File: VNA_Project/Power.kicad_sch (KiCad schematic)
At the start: 35 parts, among them J201 USB_C_Receptacle_USB2.0_16P, J202 Jack-DC, U201 AP7375, U202 USBLC6-2SC6, U203 TLV62569DBV, U204 HT7533-1, U6 MIC5501-3.0YM5

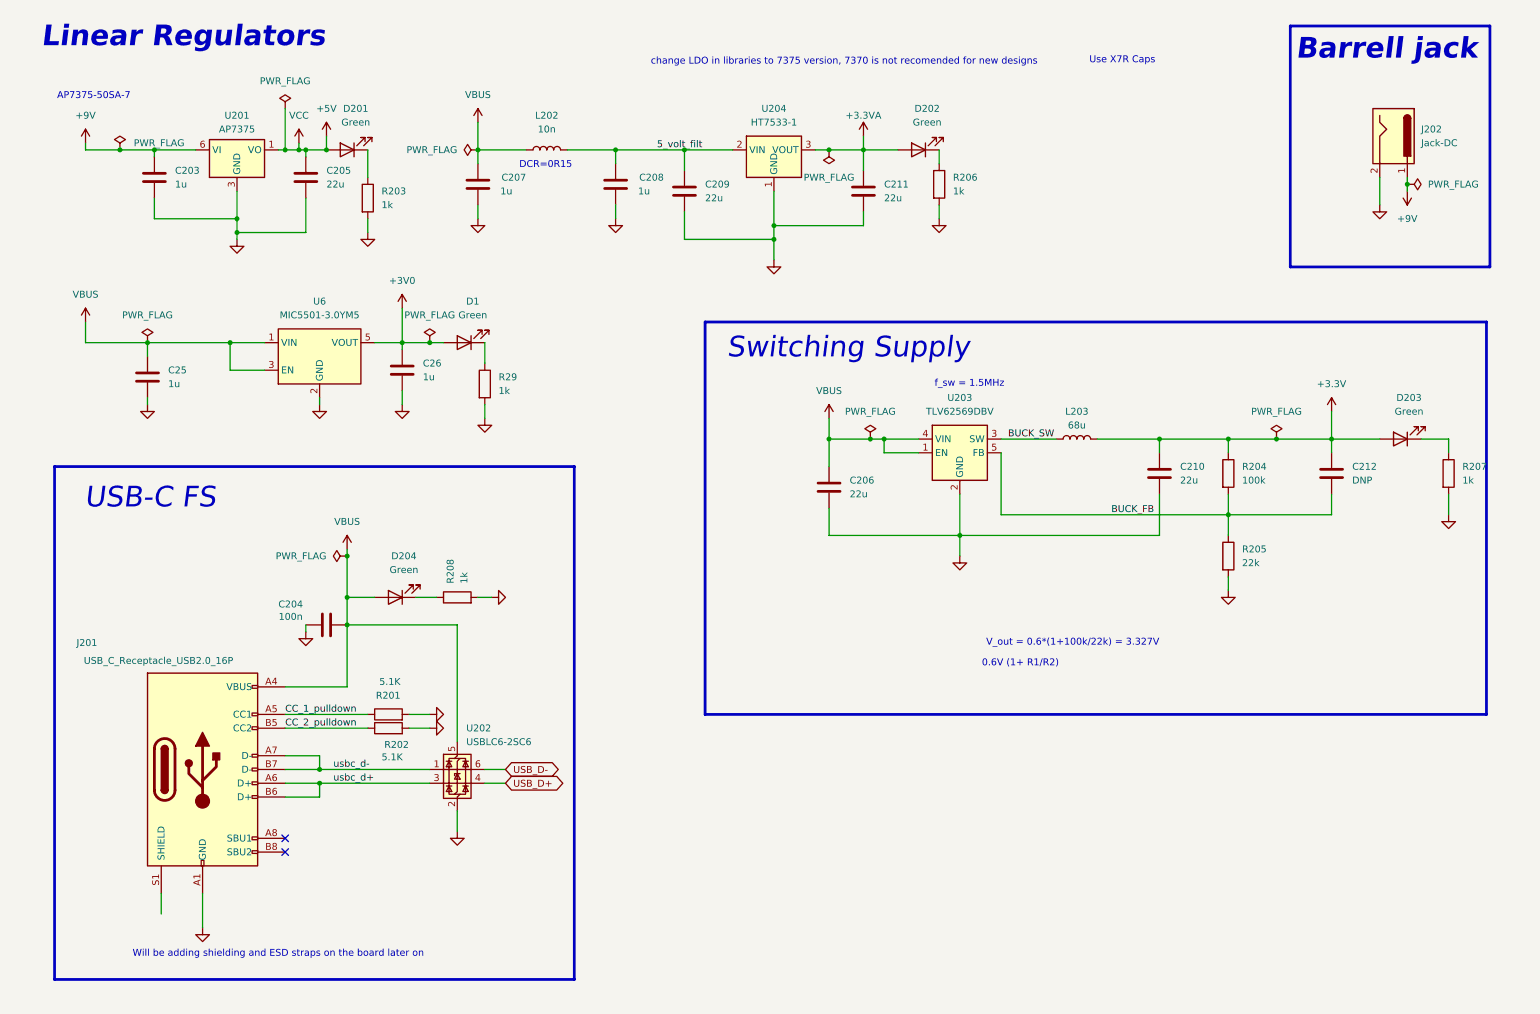
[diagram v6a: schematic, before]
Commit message: finishing up front end
refining Non RF front end
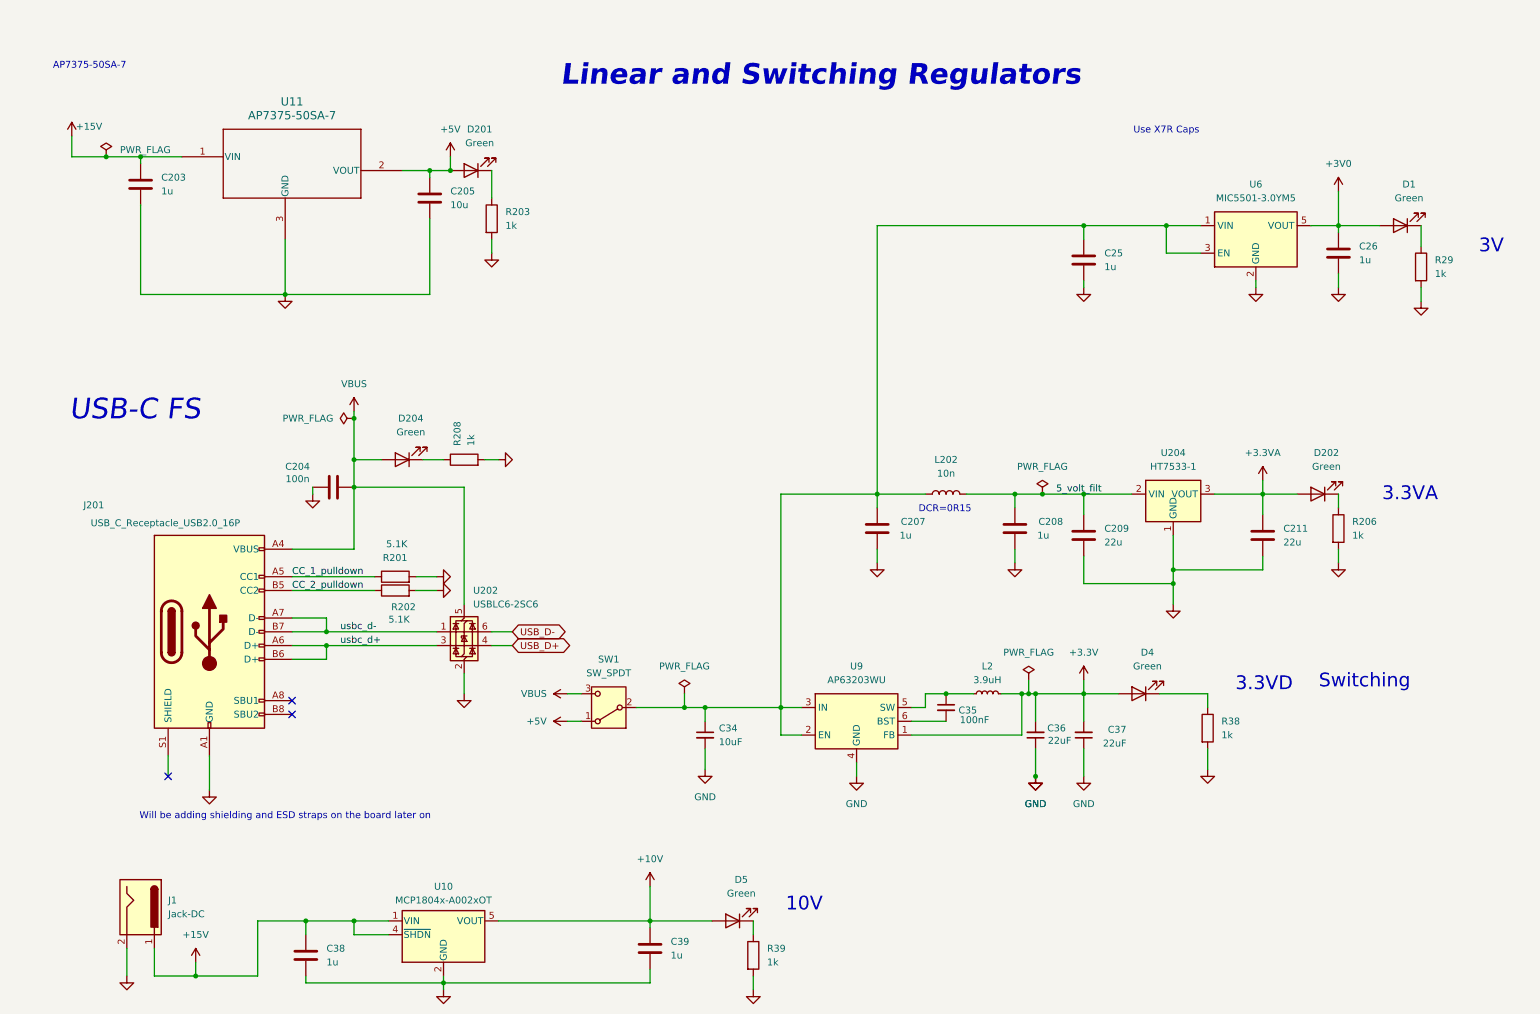
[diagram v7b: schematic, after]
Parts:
- removed C206, C210: 22u, Capacitor_SMD:C_0603_1608Metric_Pad1.08x0.95mm_HandSolder, symbol Device:C
- removed C212: DNP, Capacitor_SMD:C_0402_1005Metric_Pad0.74x0.62mm_HandSolder, symbol Device:C
- removed D203: Green, LED_SMD:LED_0402_1005Metric_Pad0.77x0.64mm_HandSolder, symbol Device:LED
- removed J202: Jack-DC, symbol Connector:Jack-DC
- removed L203: 68u, Inductor_SMD:L_0603_1608Metric_Pad1.05x0.95mm_HandSolder, symbol Device:L
- removed R204: 100k, Resistor_SMD:R_0402_1005Metric_Pad0.72x0.64mm_HandSolder, symbol Device:R
- removed R205: 22k, Resistor_SMD:R_0402_1005Metric_Pad0.72x0.64mm_HandSolder, symbol Device:R
- removed R207: 1k, Resistor_SMD:R_0402_1005Metric_Pad0.72x0.64mm_HandSolder, symbol Device:R
- removed U201: AP7375, Package_DFN_QFN:DFN-6-1EP_2x2mm_P0.65mm_EP1.01x1.7mm, symbol Regulator_Linear:AP7370-50FDC
- removed U203: TLV62569DBV, Package_TO_SOT_SMD:SOT-23-5, symbol Regulator_Switching:TLV62569DBV
- added C34: 10uF, Capacitor_SMD:C_1206_3216Metric_Pad1.33x1.80mm_HandSolder, symbol Device:C_Small
- added C35: 100nF, Capacitor_SMD:C_1206_3216Metric_Pad1.33x1.80mm_HandSolder, symbol Device:C_Small
- added C36, C37: 22uF, Capacitor_SMD:C_1206_3216Metric_Pad1.33x1.80mm_HandSolder, symbol Device:C_Small
- added C38, C39: 1u, symbol Device:C
- added D4, D5: Green, symbol Device:LED
- added J1: Jack-DC, symbol Connector:Jack-DC
- added L2: 3.9uH, Inductor_SMD:L_Bourns_SDR0604, symbol Device:L_Small
- added R38: 1k, Resistor_SMD:R_0402_1005Metric_Pad0.72x0.64mm_HandSolder, symbol Device:R
- added R39: 1k, symbol Device:R
- added SW1: SW_SPDT, Button_Switch_THT:SW_Slide_SPDT_Straight_CK_OS102011MS2Q, symbol Switch:SW_SPDT
- added U10: MCP1804x-A002xOT, Package_TO_SOT_SMD:SOT-23-5, symbol Regulator_Linear:MCP1804x-A002xOT
- added U11: AP7375-50SA-7, SOT23_DIO_DOD, symbol Non_KiCad_Symbols:AP7375-50SA-7
- added U9: AP63203WU, Package_TO_SOT_SMD:TSOT-23-6, symbol Regulator_Switching:AP63203WU
- C205: value 22u -> 10u
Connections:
- net +3.3V: now also C36.2, C37.2, D4.2 (A), L2.2, U9.1 (FB)
- net +5V: now also SW1.1 (A), U11.2 (VOUT)
- net GND: now also C34.2, C36.1, C37.1, C38.2, C39.2, J1.2, R38.2, R39.2, U10.2 (GND), U11.3 (GND), U9.4 (GND)
- net VBUS: now also SW1.3 (C); no longer C207.1, C25.1, L202.1, U6.1 (VIN), U6.3 (EN)
- net +9V renamed +15V
- net +15V: now also C38.1, J1.1, U10.1 (VIN), U10.4 (~{SHDN}), U11.1 (VIN)
- new net: C207.1, C25.1, C34.1, L202.1, SW1.2 (B), U6.1 (VIN), U6.3 (EN), U9.2 (EN), U9.3 (IN)
- new net: C35.1, L2.1, U9.5 (SW)
- new net: C35.2, U9.6 (BST)
- new net: D4.1 (K), R38.1
- new net: D5.1 (K), R39.1
- new net +10V: C39.1, D5.2 (A), U10.5 (VOUT)
- no-connect marks 2 -> 3
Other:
- note added: "10V"
- note added: "3.3VA"
- note added: "3.3VD"
- note added: "3V"
- note added: "Linear and Switching Regulators"
- note added: "Switching"
- note removed: "0.6V (1+ R1/R2)"
- note removed: "Barrell jack"
- note removed: "Linear Regulators"
- note removed: "Switching Supply"
- note removed: "V_out = 0.6*(1+100k/22k) = 3.327V"
- note removed: "change LDO in libraries to 7375 version, 7370 is not recomended for new designs"
- note removed: "f_sw = 1.5MHz"
- moved on the sheet: C203, C204, C205, C207, C208, C209, C211, C25, C26, D1, D201, D202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

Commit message: AA filtering
redoing AA filtering
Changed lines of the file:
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@@
 	(wire
 		(pts
-			(xy 96.52 129.54) (xy 100.33 129.54)
+			(xy 96.52 129.54) (xy 129.54 129.54)
 		)
 		(stroke
@@
 	(wire
 		(pts
-			(xy 96.52 127) (xy 100.33 127)
+			(xy 96.52 127) (xy 129.54 127)
 		)
 		(stroke
@@
 	(wire
 		(pts
-			(xy 91.44 121.92) (xy 91.44 100.33)
+			(xy 91.44 100.33) (xy 91.44 121.92)
 		)
 		(stroke
@@
 	(global_label "USB_D-"
 		(shape bidirectional)
-		(at 100.33 127 0)
+		(at 129.54 127 0)
 		(fields_autoplaced yes)
 		(effects
@@
 		)
 		(property "Intersheetrefs" "${INTERSHEET_REFS}"
-			(at 112.0465 127 0)
+			(at 141.2565 127 0)
 			(effects
 				(font
@@
 	(global_label "USB_D+"
 		(shape bidirectional)
-		(at 100.33 129.54 0)
+		(at 129.54 129.54 0)
 		(fields_autoplaced yes)
 		(effects
@@
 		)
 		(property "Intersheetrefs" "${INTERSHEET_REFS}"
-			(at 112.0465 129.54 0)
+			(at 141.2565 129.54 0)
 			(effects
 				(font
